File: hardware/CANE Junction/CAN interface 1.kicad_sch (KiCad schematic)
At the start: 19 parts, among them J1 glv, U201 TL432DBZ, U202 TPS7B4254, U203 ISO1044BD, U204 ISOM8600, U205 PUCC33420QRAQRQ1

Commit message: CANE put together and seemingly not exploding
meow meow meow
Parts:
- added R5: 40.2k, Resistor_SMD:R_0805_2012Metric_Pad1.20x1.40mm_HandSolder, symbol Device:R_Small_US
- J1: footprint Connector_Molex:Molex_Micro-Fit_3.0_43650-0400_1x04_P3.00mm_Horizontal -> Connector_Molex:Molex_Micro-Fit_3.0_43045-0400_2x02_P3.00mm_Horizontal
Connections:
- net IL+ is gone; now on net LV+: J1.2 (Pin_2)
- net IL- is gone; now on net LV-: J1.1 (Pin_1)
- net 5v: no longer C203.1, C204.1, RN1.8 (R4.2), U202.1 (OUT), U202.4 (FB), U203.8 (VCC2), U205.2 (VINP)
- net 5v_ldo_ref: now also RN1.1 (R1.1); no longer RN1.4 (R2.2)
- net CAN+: now also FL201.4; no longer FL201.1
- net CAN-: now also FL201.1; no longer FL201.4
- net LV+: now also RN1.8 (R4.2); no longer RN1.6 (R3.2)
- net LV-: now also RN1.3 (R2.1); no longer RN1.1 (R1.1)
- net at CR201.2, FL201.3: now also U203.6 (CANH); no longer U203.5 (CANL)
- net at CR201.1, FL201.2: now also U203.5 (CANL); no longer U203.6 (CANH)
- net at D201.2 (A): now also RN1.7 (R4.1); no longer RN1.5 (R3.1)
- net at U205.1 (EN/FLT): now also R5.1; no longer RN1.7 (R4.1)
- net at RN1.2 (R1.2), U201.1 (REF): now also RN1.4 (R2.2); no longer RN1.3 (R2.1)
- new net GLV_5v: C203.1, C204.1, R5.2, U202.1 (OUT), U202.4 (FB), U203.8 (VCC2), U205.2 (VINP)
- no-connect marks 0 -> 2

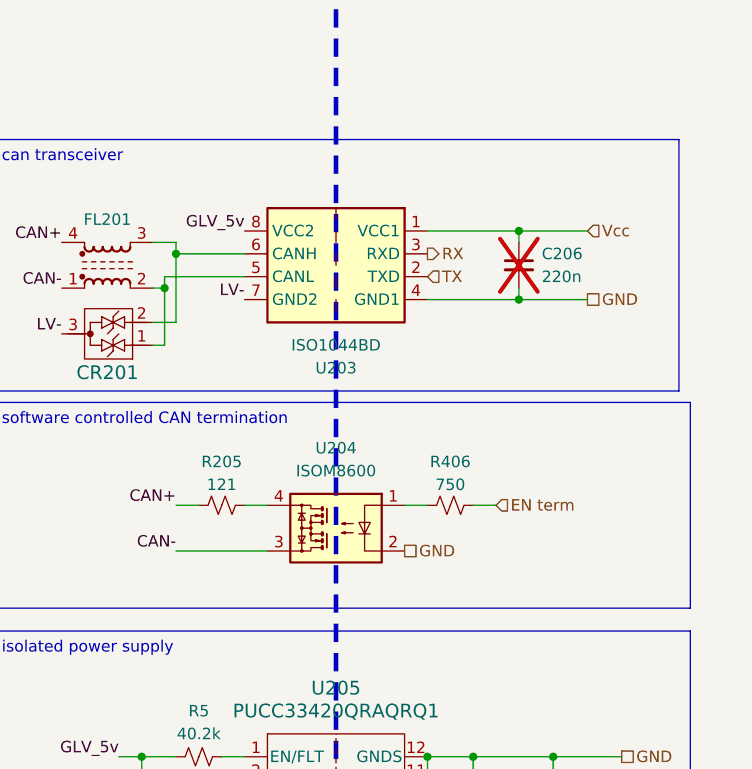
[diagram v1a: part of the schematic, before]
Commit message: transcevier out of stock, swapped out
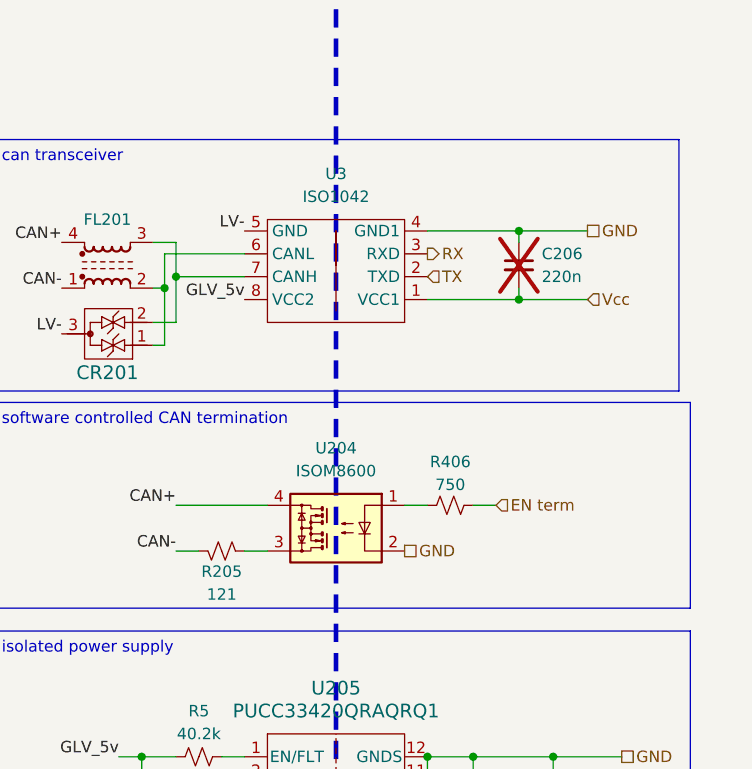
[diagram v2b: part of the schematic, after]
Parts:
- removed U203: ISO1044BD, Package_SO:SOIC-8_5.3x5.3mm_P1.27mm, symbol Interface_CAN_LIN:ISO1044BD
- added U3: ISO1042, Package_SO:SOIC-8_7.5x5.85mm_P1.27mm, symbol zzLocalLibrary:ISO1042
- J1: mouser (none) -> https://www.mouser.com/ProductDetail/Molex/43045-0421?qs=Ue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
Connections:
- net CAN+: now also U204.4; no longer R205.1
- net CAN-: now also R205.1; no longer U204.3
- net GLV_5v: now also U3.8 (VCC2)
- net GND: now also C206.1, U3.4 (GND1); no longer C206.2
- net LV-: now also U3.5 (GND)
- net RX: now also U3.3 (RXD)
- net TX: now also U3.2 (TXD)
- net Vcc: now also C206.2, U3.1 (VCC1); no longer C206.1
- net at CR201.1, FL201.2: now also U3.6 (CANL)
- net at CR201.2, FL201.3: now also U3.7 (CANH)
- net at R205.2: now also U204.3; no longer U204.4
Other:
- moved on the sheet: R205

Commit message: mmm
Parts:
- removed C201, C202, C203, C206, C207: 220n, Capacitor_SMD:C_0805_2012Metric_Pad1.18x1.45mm_HandSolder, symbol Device:C_Small
- removed C204, C205: 22u, Capacitor_SMD:C_0805_2012Metric_Pad1.18x1.45mm_HandSolder, symbol Device:C_Small
- removed CR201: ESD2CAN36DBZRQ1, Package_TO_SOT_SMD:TSOT-23_HandSoldering, symbol zzLocalLibrary:ESD2CAN36DBZRQ1
- removed D201: TS4148, Diode_SMD:D_0805_2012Metric_Pad1.15x1.40mm_HandSolder, symbol Device:D_Small
- removed FL201: Choke_CommonMode_FerriteCore_1243, zzLocalLibraries-Footprints:L_CommonModeChoke_Coilcraft_1812CAN, symbol Filter:Choke_CommonMode_FerriteCore_1243
- removed J1: glv, Connector_Molex:Molex_Micro-Fit_3.0_43045-0400_2x02_P3.00mm_Horizontal, symbol Connector_Generic:Conn_01x04
- removed R205: 121, Resistor_SMD:R_0805_2012Metric_Pad1.20x1.40mm_HandSolder, symbol Device:R_Small_US
- removed R406: 750, Resistor_SMD:R_0805_2012Metric_Pad1.20x1.40mm_HandSolder, symbol Device:R_Small_US
- removed R5: 40.2k, Resistor_SMD:R_0805_2012Metric_Pad1.20x1.40mm_HandSolder, symbol Device:R_Small_US
- removed RN1: 56K, zzLocalLibraries-Footprints:R_array_YCJ164_4, symbol Device:R_Pack04_SIP_Split
- removed U201: TL432DBZ, Package_TO_SOT_SMD:SOT-23-3, symbol Reference_Voltage:TL432DBZ
- removed U202: TPS7B4254, Package_SO:Texas_R-PDSO-G8_EP2.95x4.9mm_Mask2.4x3.1mm, symbol zzLocalLibrary:TPS7B4252
- removed U204: ISOM8600, zzLocalLibraries-Footprints:SOIC4_DFG_TEX-M, symbol zzLocalLibrary:ISOM8600
- removed U205: PUCC33420QRAQRQ1, zzLocalLibraries-Footprints:VSON-FCRLF12_RAQ_TEX, symbol zzLocalLibrary:PUCC33420QRAQRQ1
- removed U3: ISO1042, Package_SO:SOIC-8_7.5x5.85mm_P1.27mm, symbol zzLocalLibrary:ISO1042
- added C101, C106: 470n, Capacitor_SMD:C_0805_2012Metric_Pad1.18x1.45mm_HandSolder, symbol Device:C_Small
- added C110, C114, C115: 220n, Capacitor_SMD:C_0805_2012Metric_Pad1.18x1.45mm_HandSolder, symbol Device:C_Small
- added C111, C112, C113: 22u, Capacitor_SMD:C_0805_2012Metric_Pad1.18x1.45mm_HandSolder, symbol Device:C_Small
- added CR101: ESD2CAN36DBZRQ1, Package_TO_SOT_SMD:TSOT-23_HandSoldering, symbol zzLocalLibrary:ESD2CAN36DBZRQ1
- added D101, D103: ES1D, Diode_SMD:D_SMA, symbol Device:D_Schottky_Small
- added FL101: Choke_CommonMode_FerriteCore_1243, Inductor_SMD:L_CommonMode_Wurth_WE-CNSW-1206, symbol Filter:Choke_CommonMode_FerriteCore_1243
- added J101: glv, Connector_Molex:Molex_Micro-Fit_3.0_43045-0400_2x02_P3.00mm_Horizontal, symbol Connector_Generic:Conn_01x04
- added L101: 10u, Inductor_SMD:L_1210_3225Metric_Pad1.42x2.65mm_HandSolder, symbol Device:L_Small
- added R101: 121, Resistor_SMD:R_0805_2012Metric_Pad1.20x1.40mm_HandSolder, symbol Device:R_Small_US
- added R102: 750, Resistor_SMD:R_0805_2012Metric_Pad1.20x1.40mm_HandSolder, symbol Device:R_Small_US
- added RN101: 20k, zzLocalLibraries-Footprints:R_array_EXB2HV_8, symbol Device:R_Pack08_Split
- added TP101: TestPoint, TestPoint:TestPoint_Pad_D1.0mm, symbol Connector:TestPoint
- added U101: AP64060ZQ, Package_TO_SOT_SMD:TSOT-23-6, symbol zzLocalLibrary:AP64060ZQ
- added U103: MCP2542FDxMF, Package_SO:SOIC-8_3.9x4.9mm_P1.27mm, symbol Interface_CAN_LIN:MCP2542FDxMF
- added U104: ISO7721D, Package_SO:SOIC-8_3.9x4.9mm_P1.27mm, symbol Isolator:ISO7721D
- added U105: ISOM8600, zzLocalLibraries-Footprints:SOIC4_DFG_TEX-M, symbol zzLocalLibrary:ISOM8600
- added U106: PUCC33420QRAQRQ1, zzLocalLibraries-Footprints:VSON-FCRLF12_RAQ_TEX, symbol zzLocalLibrary:PUCC33420QRAQRQ1
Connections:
- net 5v: now also C113.2, C115.2, U106.7 (SEL), U106.8 (VCC)
- net CAN+: now also FL101.4, J101.3 (Pin_3), U105.4
- net CAN-: now also FL101.1, J101.4 (Pin_4), R101.1
- net EN term: now also R102.2
- net GLV_5v: now also C111.1, C112.1, L101.1, RN101.16 (R1.2), RN101.9 (R8.2), TP101.1, U103.3 (VDD), U103.5 (VIO), U104.1 (VCC1), U106.2 (VINP)
- net GND: now also C113.1, C114.2, C115.1, U104.5 (GND2), U105.2, U106.10 (GNDS), U106.11 (GNDS), U106.12 (GNDS), U106.9 (GNDS)
- net LV+: now also D101.2 (A), J101.2 (Pin_2)
- net LV-: now also C101.2, C106.2, C111.2, C112.2, CR101.3, D103.2 (A), J101.1 (Pin_1), RN101.5 (R5.1), U101.2 (GND), U103.2 (VSS), U103.8 (STBY), U103.9 (VSS), U104.4 (GND1), U106.3 (GNDP), U106.4 (GNDP), U106.5 (GNDP), U106.6 (GNDP)
- net RX: now also U104.6 (OUTB)
- net TX: now also U104.7 (INA)
- net Vcc: now also C114.1, U104.8 (VCC2)
- new net: U103.1 (TXD), U104.2 (OUTA)
- new net: U103.4 (RXD), U104.3 (INB)
- new net: CR101.1, FL101.2, U103.6 (CANL)
- new net: CR101.2, FL101.3, U103.7 (CANH)
- new net: C110.2, D103.1 (K), L101.2, U101.6 (SW)
- new net: RN101.13 (R4.2), RN101.3 (R3.1)
- new net: RN101.12 (R5.2), RN101.4 (R4.1), U101.3 (FB)
- new net: RN101.8 (R8.1), U106.1 (EN/FLT)
- new net: C101.1, C106.1, D101.1 (K), U101.4 (EN), U101.5 (Vin)
- new net: RN101.1 (R1.1), RN101.15 (R2.2)
- new net: RN101.14 (R3.2), RN101.2 (R2.1)
- new net: C110.1, U101.1 (BST)
- new net: R102.1, U105.1
- new net: R101.2, U105.3
- no-connect marks 2 -> 0

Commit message: tmb pci technology
doner motherboard generator
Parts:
- removed D103: ES1D, Diode_SMD:D_SMA, symbol Device:D_Schottky_Small
- removed U103: MCP2542FDxMF, Package_SO:SOIC-8_3.9x4.9mm_P1.27mm, symbol Interface_CAN_LIN:MCP2542FDxMF
- removed U104: ISO7721D, Package_SO:SOIC-8_3.9x4.9mm_P1.27mm, symbol Isolator:ISO7721D
- added C110: 220n, Capacitor_SMD:C_0805_2012Metric_Pad1.18x1.45mm_HandSolder, symbol Device:C_Small
- added D103: TS4148, Diode_SMD:D_0805_2012Metric_Pad1.15x1.40mm_HandSolder, symbol Device:D_Small
- added unit 7 of RN101
- added unit 6 of RN101
- added U103: ISO1044BD, Package_SO:SOIC-8_5.3x6.2mm_P1.27mm, symbol Interface_CAN_LIN:ISO1044BD
- added U106: NCP163ASN330T1G, Package_TO_SOT_SMD:SOT-23-5_HandSoldering, symbol Regulator_Linear:NCP163ASN330T1G
- CR101: mouser (none) -> https://www.mouser.com/ProductDetail/Texas-Instruments/ESD2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
- J101: mouser https://www.mouser.com/ProductDetail/Molex/43045-0421?qs=Ue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 -> https://www.mouser.com/ProductDetail/Molex/43045-0400?qs=Ue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
- TP101: now not fitted; now left out of the parts list
- renumbered C106 to C102, C110 to C103, C111 to C104, C112 to C105, C113 to C106, C114 to C108, C115 to C109, U105 to U104, U106 to U105
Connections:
- net CAN+: now also FL101.1; no longer FL101.4
- net CAN-: now also FL101.4; no longer FL101.1
- net GLV_5v: now also RN101.13 (R4.2), C110.1, U103.8 (VCC2); no longer RN101.9 (R8.2)
- net GND: now also U103.4 (GND1), U106.2 (GND)
- net LV-: now also RN101.8 (R8.1), C110.2, D103.2 (A), U103.7 (GND2); no longer RN101.5 (R5.1)
- net RX: now also U103.3 (RXD)
- net TX: now also U103.2 (TXD)
- net Vcc: now also U103.1 (VCC1)
- net C_P: now reaches CR101.1, FL101.2
- net C_P: now also U103.6 (CANH)
- net C_N: now reaches CR101.2, FL101.3
- net C_N: now also U103.5 (CANL)
- net at C103.2, L101.2, U101.6 (SW): now also D103.1 (K)
- net at RN101.3 (R3.1): no longer RN101.13 (R4.2)
- net at U105.1 (EN/FLT): now also RN101.1 (R1.1); no longer RN101.8 (R8.1)
- net at RN101.15 (R2.2): no longer RN101.1 (R1.1)
- net at RN101.2 (R2.1): no longer RN101.14 (R3.2)
- net 5v: no longer names the net of C106.2, C109.2, U105.7 (SEL), U105.8 (VCC)
- net 5v: now also U106.1 (VIN), U106.3 (EN)
- new net: RN101.4 (R4.1), RN101.5 (R5.1)
- new net: RN101.10 (R7.2), RN101.9 (R8.2), U101.3 (FB)
- new net: RN101.11 (R6.2), RN101.12 (R5.2)
- new net: RN101.6 (R6.1), RN101.7 (R7.1)
- new net 3v3: U106.5 (VOUT)
- no-connect marks 0 -> 4
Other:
- moved on the sheet: CR101, FL101, RN101A, RN101B, RN101C, RN101D, RN101E, RN101H
